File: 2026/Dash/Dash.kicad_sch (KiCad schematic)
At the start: 76 parts, among them IC1 ESP32-S3-WROOM-1-N8R8, IC2 CP2102N-A02-GQFN28, IC3 TLP175A_TPL,E, IC4 TPS2116DRLR, IC5 MIC37100-3.3WS, IC6 TLC5955RTQT, IC7 TLC5955RTQT, J1 ESP_USB, J5 Conn_01x40_Pin, Q1 MMBT2222LT1G, Q2 MMBT2222LT1G, U1 USBLC6-2SC6, U2 SN65HVD230

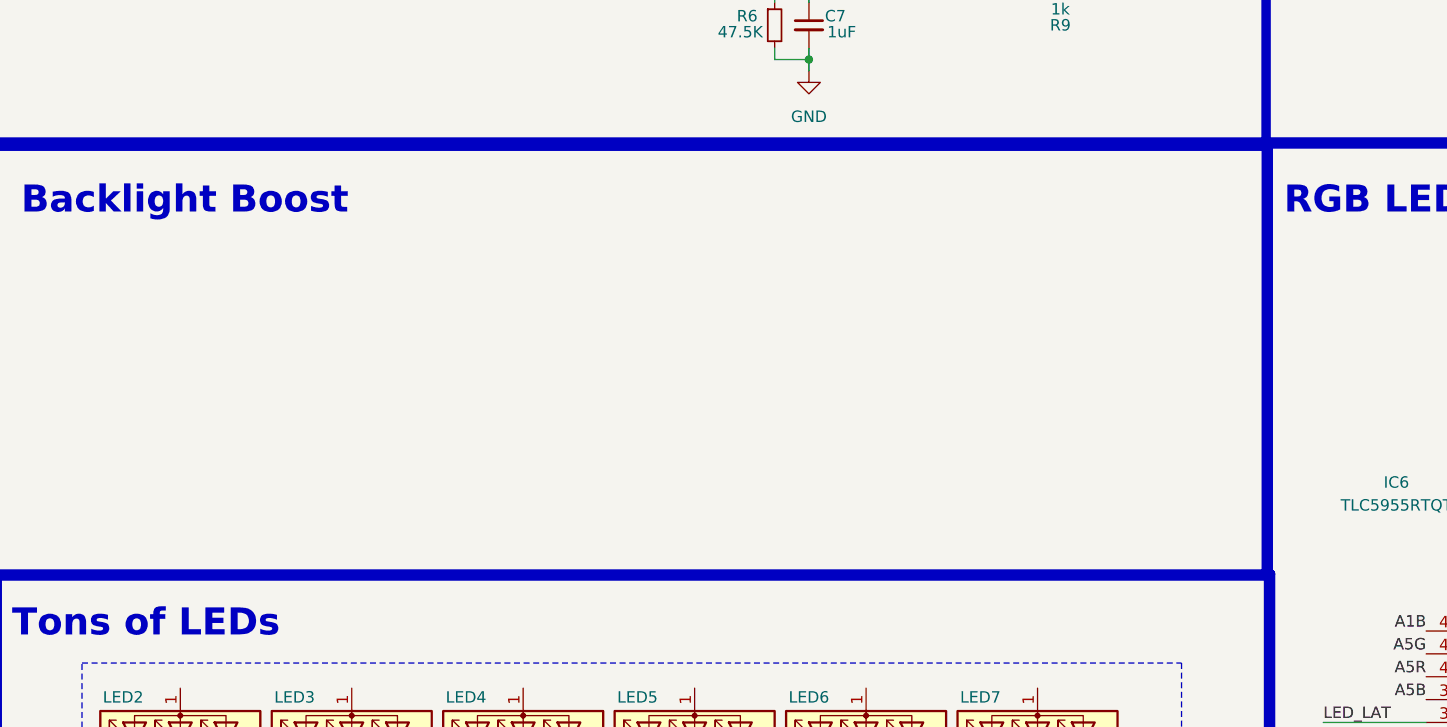
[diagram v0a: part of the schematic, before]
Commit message: Added Backlight boost to dash Sch
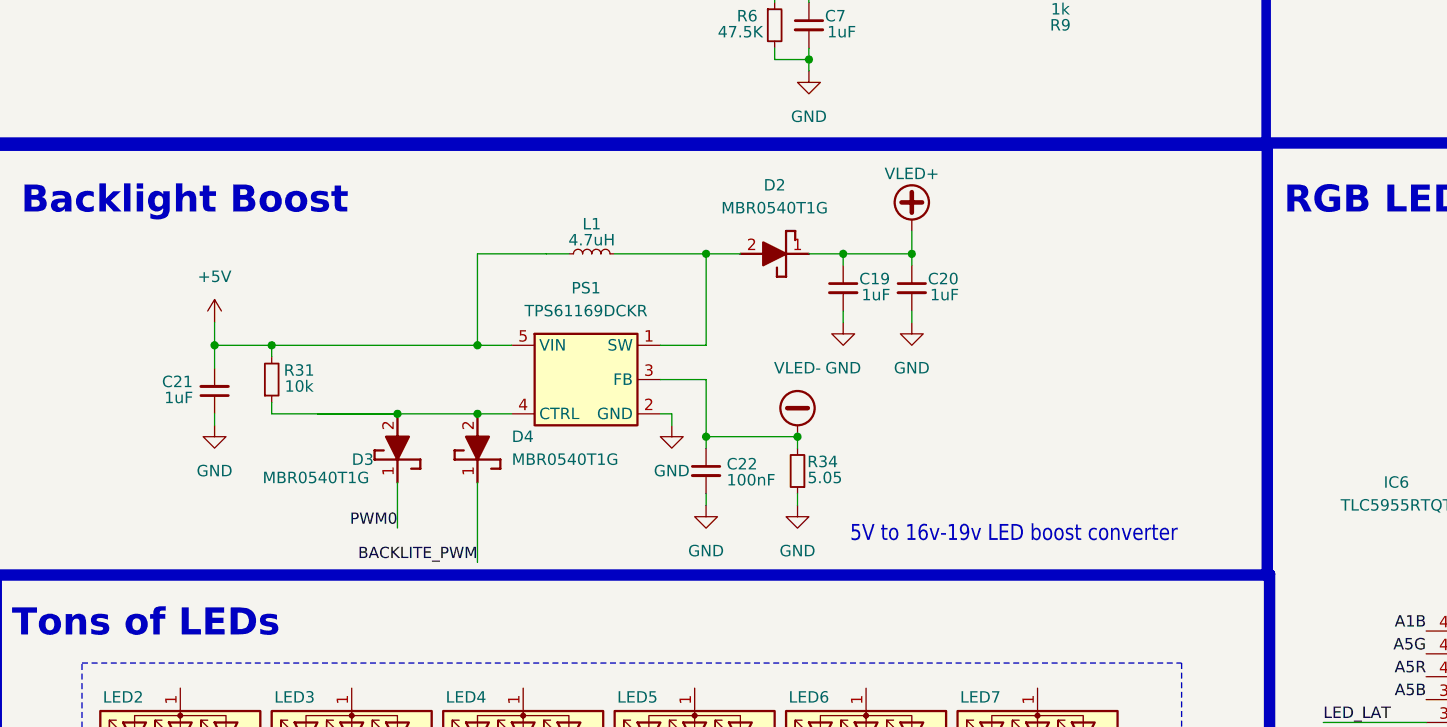
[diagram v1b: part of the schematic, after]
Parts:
- added C19, C20, C21: 1uF, Capacitor_SMD:C_0603_1608Metric, symbol Device:C_Small
- added C22: 100nF, Capacitor_SMD:C_0603_1608Metric, symbol Device:C_Small
- added D2, D3, D4: MBR0540T1G, SDM_MiscFootprint:SOD3716X135N, symbol SDM_DIODES:MBR0540T1G
- added L1: 4.7uH, SDM_MiscFootprint:BWVS006060454R7ML1, symbol Device:L_Small
- added PS1: TPS61169DCKR, SDM_MiscFootprint:SOT65P210X110-5N, symbol SDM_VOLTAGE_REGULATORS:TPS61169DCKR
- added R31: 10k, Resistor_SMD:R_0603_1608Metric, symbol Device:R_Small
- added R34: 5.05, Resistor_SMD:R_0603_1608Metric, symbol Device:R_Small
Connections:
- net +5V: now also C21.2, L1.2, PS1.5 (VIN), R31.2
- net GND: now also C19.2, C20.2, C21.1, C22.2, PS1.2 (GND), R34.1
- net VLED+: now also C19.1, C20.1, D2.1 (K)
- net VLED-: now also C22.1, PS1.3 (FB), R34.2
- new net: D3.2 (A), D4.2 (A), PS1.4 (CTRL), R31.1
- new net: D2.2 (A), L1.1, PS1.1 (SW)
- new net BACKLITE_PWM: D4.1 (K)
- new net PWM0: D3.1 (K)
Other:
- note added: "5V to 16v-19v LED boost converter"

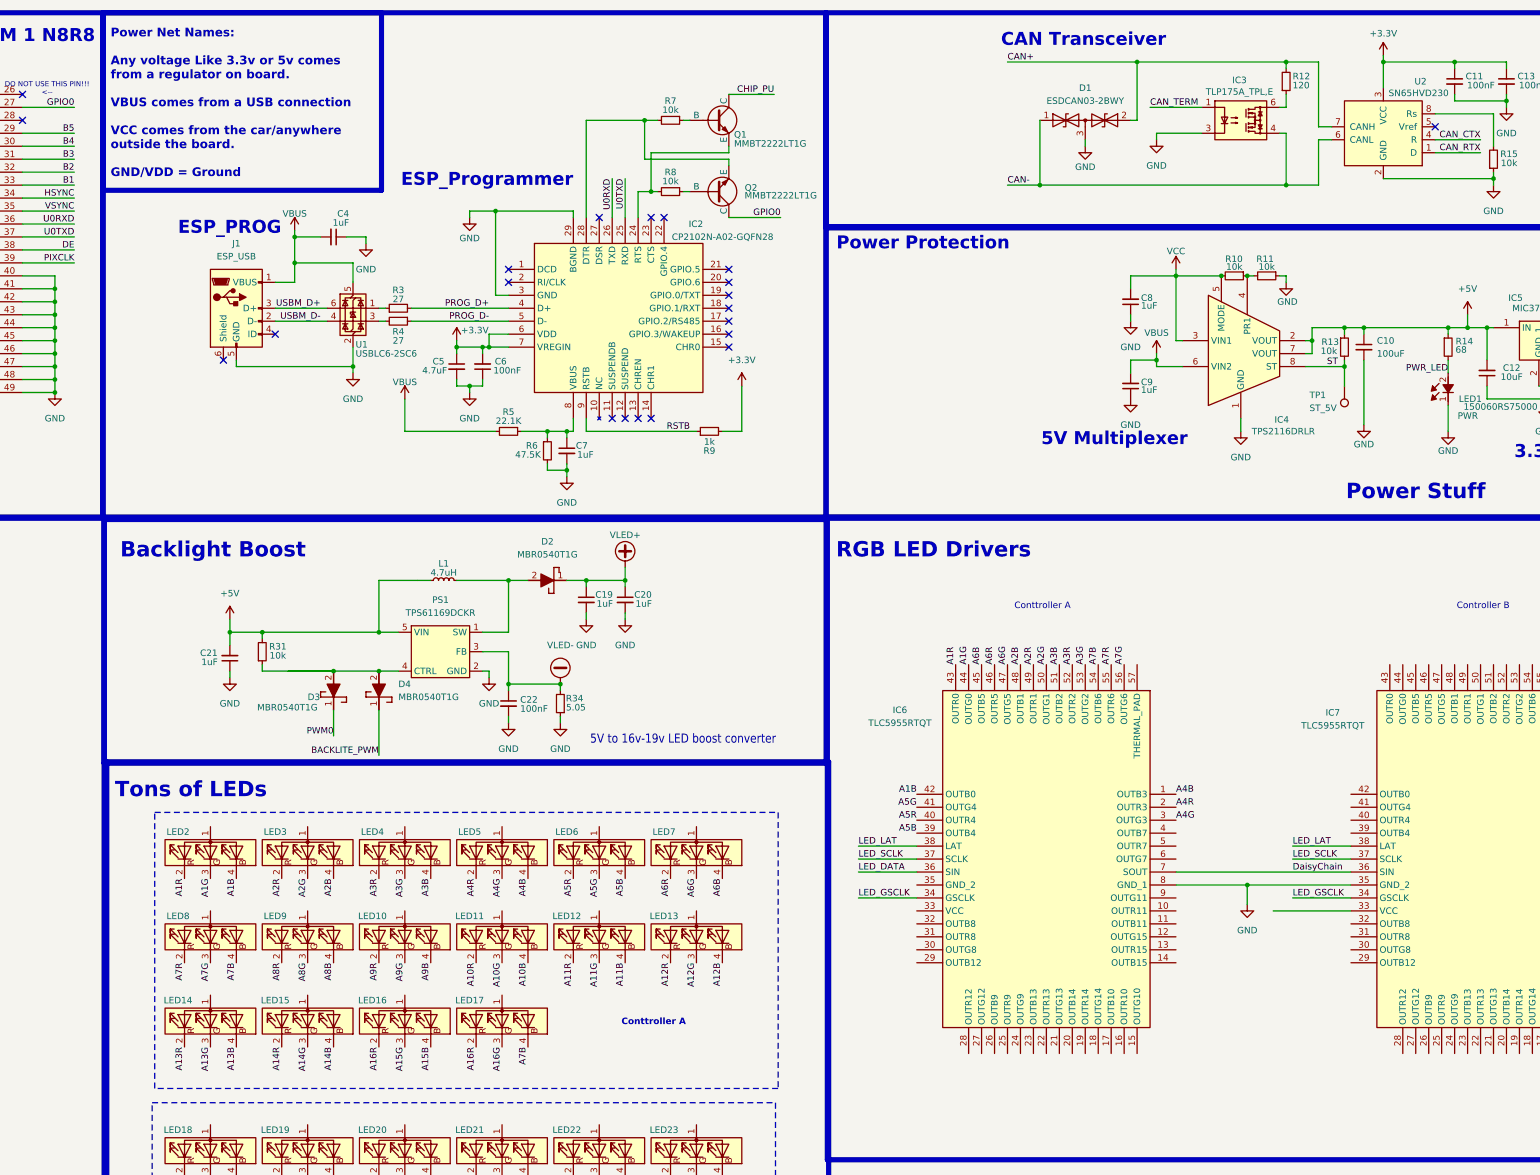
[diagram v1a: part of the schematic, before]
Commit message: Dash Sch Edits
Moved to USB-C
Progress on RGB LED nets
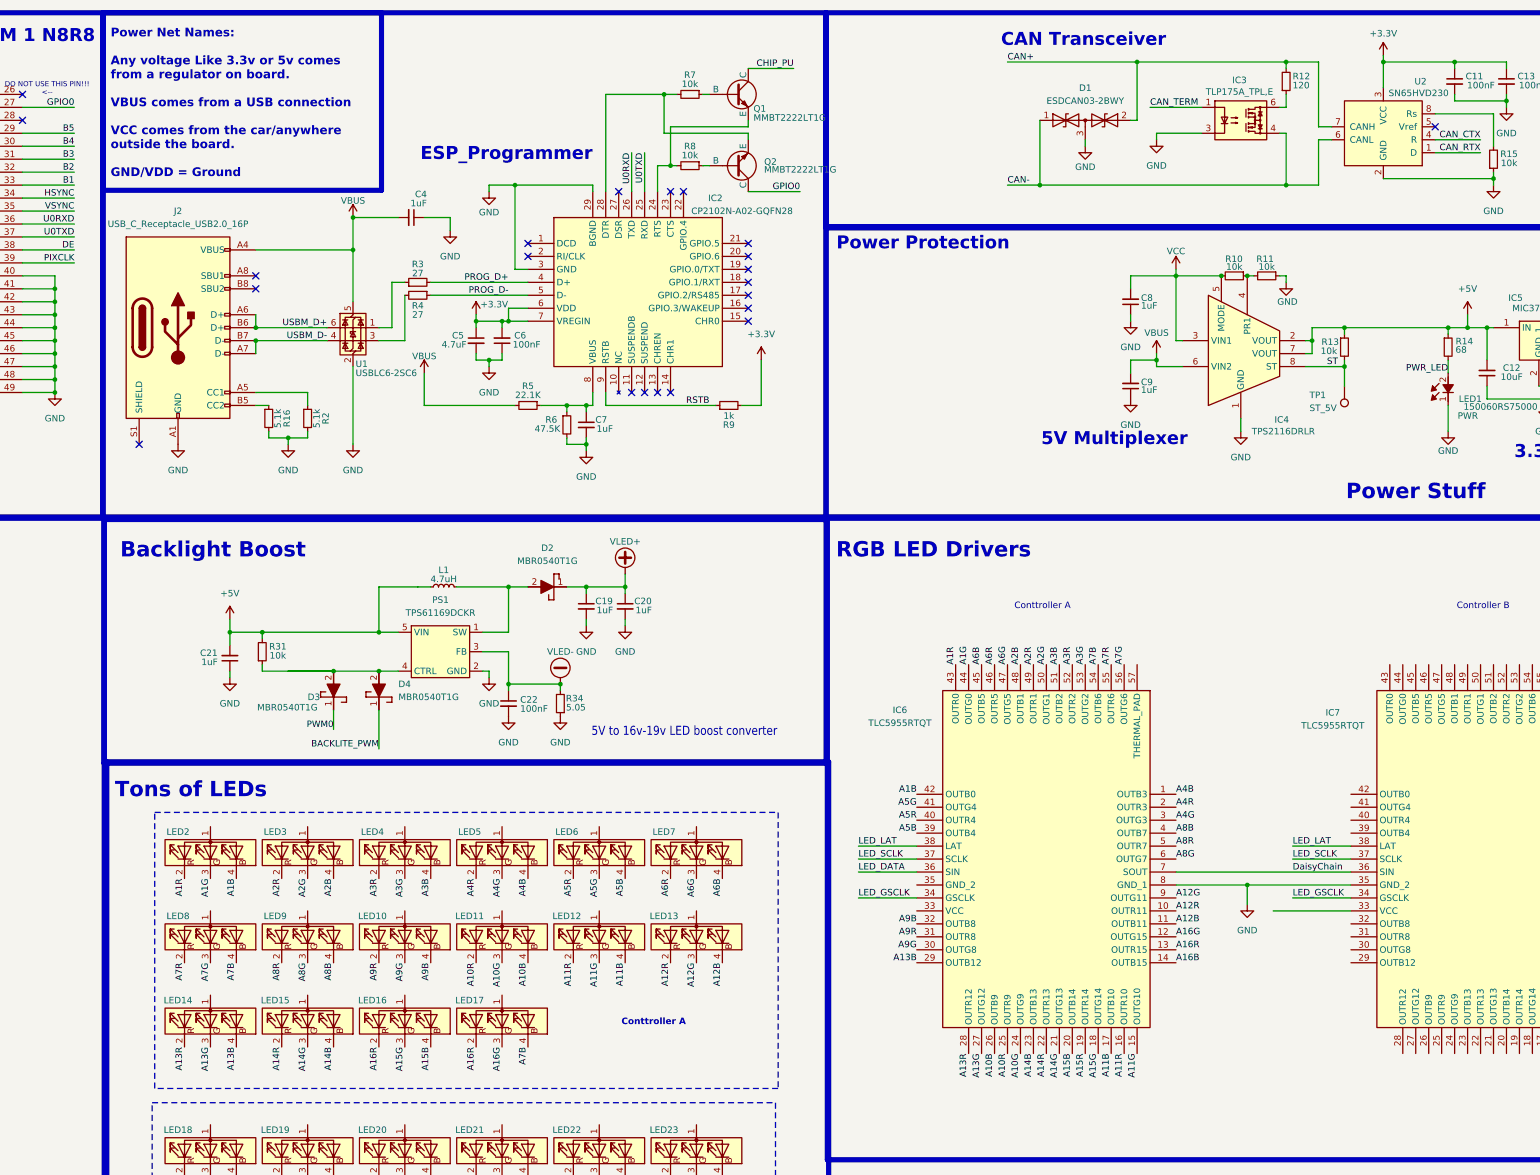
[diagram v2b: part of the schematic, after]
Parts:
- removed C10: 100uF, Capacitor_SMD:C_0603_1608Metric, symbol Device:C_Small
- removed J1: ESP_USB, Connector_USB:USB_Micro-B_Molex-105017-0001, symbol Connector:USB_B_Micro
- added J2: USB_C_Receptacle_USB2.0_16P, SDM_MiscFootprint:USB_C_Receptacle_16P, symbol Connector:USB_C_Receptacle_USB2.0_16P
- added R16, R2: 5.1k, Resistor_SMD:R_0603_1608Metric, symbol Device:R_Small
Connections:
- net A10B: now also IC6.26 (OUTB9)
- net A10G: now also IC6.24 (OUTG9)
- net A10R: now also IC6.25 (OUTR9)
- net A11B: now also IC6.17 (OUTB10)
- net A11G: now also IC6.15 (OUTG10)
- net A11R: now also IC6.16 (OUTR10)
- net A12B: now also IC6.11 (OUTB11)
- net A12G: now also IC6.9 (OUTG11)
- net A12R: now also IC6.10 (OUTR11)
- net A13B: now also IC6.29 (OUTB12)
- net A13G: now also IC6.27 (OUTG12)
- net A13R: now also IC6.28 (OUTR12)
- net A14B: now also IC6.23 (OUTB13)
- net A14G: now also IC6.21 (OUTG13)
- net A14R: now also IC6.22 (OUTR13)
- net A15B: now also IC6.20 (OUTB14)
- net A15G: now also IC6.18 (OUTG14)
- net A16G: now also IC6.12 (OUTG15)
- net A16R: now also IC6.13 (OUTR15)
- net A8B: now also IC6.4 (OUTB7)
- net A8G: now also IC6.6 (OUTG7)
- net A8R: now also IC6.5 (OUTR7)
- net A9B: now also IC6.32 (OUTB8)
- net A9G: now also IC6.30 (OUTG8)
- net A9R: now also IC6.31 (OUTR8)
- net GND: now also J2.A1 (GND), J2.A12 (GND), J2.B1 (GND), J2.B12 (GND), R16.2, R2.2
- net USBM_D+: now also J2.A6 (D+), J2.B6 (D+)
- net USBM_D-: now also J2.A7 (D-), J2.B7 (D-)
- net VBUS: now also J2.A4 (VBUS), J2.A9 (VBUS), J2.B4 (VBUS), J2.B9 (VBUS)
- net A16B: now reaches IC6.14 (OUTB15)
- net A15R: now reaches IC6.19 (OUTR14)
- new net: J2.A5 (CC1), R2.1
- new net: J2.B5 (CC2), R16.1
- no-connect marks 23 -> 24
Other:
- note removed: "ESP_PROG"
- moved on the sheet: C19, C20, C4, C5, C6, C7, D2, IC2, L1, Q1, Q2, R3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
